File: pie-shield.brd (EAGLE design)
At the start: 25 x 25.2 mm, 20 parts, among them IC4 NRF24L01SMD, Q2 3.2X2.5CRYSTAL

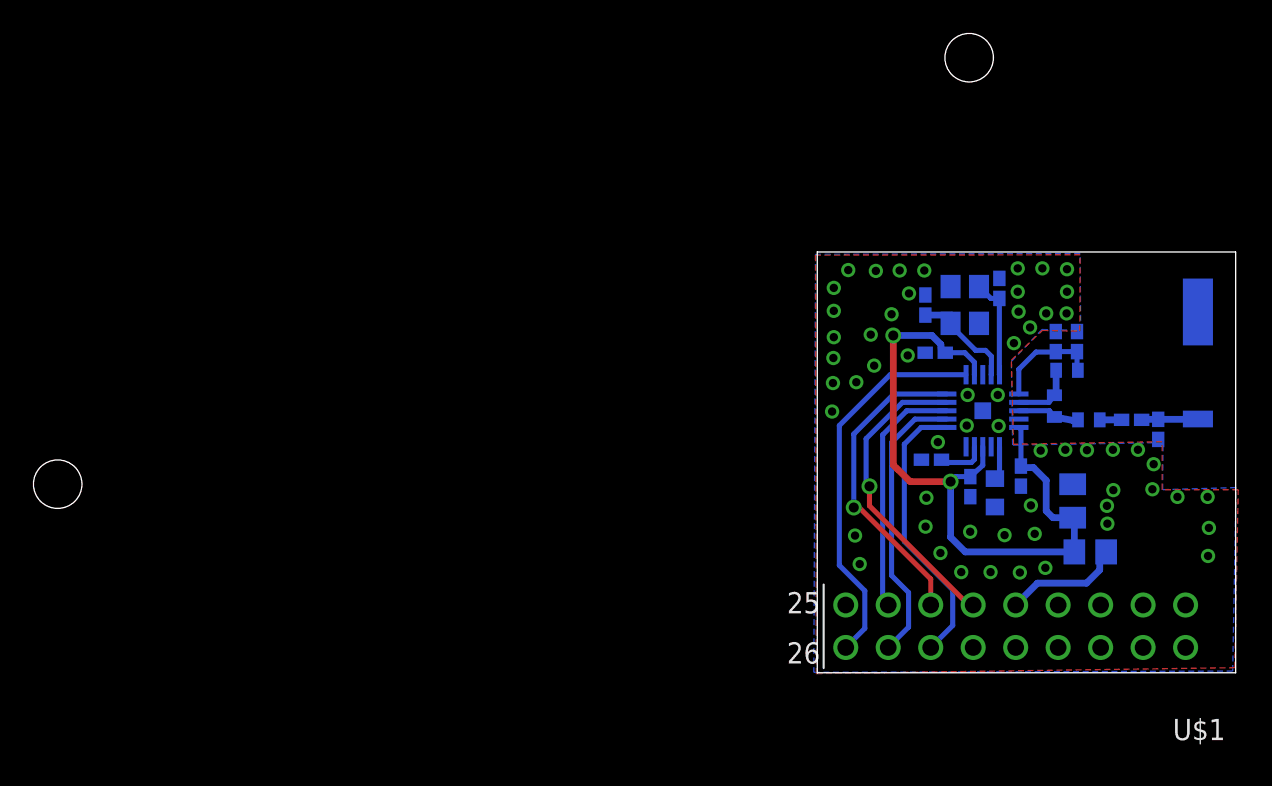
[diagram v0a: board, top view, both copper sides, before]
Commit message: fixed drill holes - removed
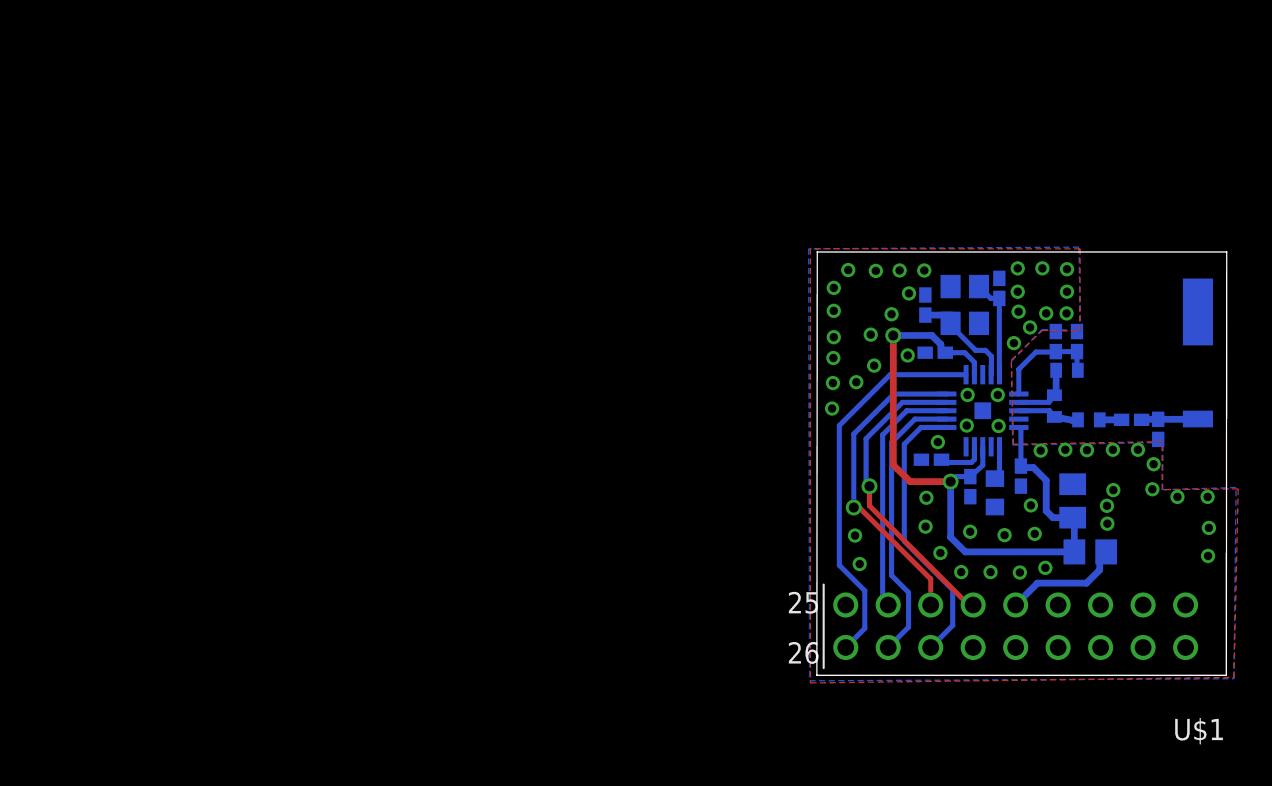
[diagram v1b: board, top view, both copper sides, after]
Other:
- board size 25 x 25.2 mm -> 24.5 x 25.3 mm
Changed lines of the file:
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@@
 <board>
 <plain>
-<wire x1="35.3314" y1="1.7526" x2="10.3152" y2="1.7526" width="0" layer="20"/>
-<wire x1="10.3152" y1="1.7526" x2="10.3152" y2="26.913" width="0" layer="20"/>
-<wire x1="10.3152" y1="26.913" x2="35.3314" y2="26.913" width="0" layer="20"/>
-<wire x1="35.3314" y1="26.913" x2="35.3314" y2="1.7526" width="0" layer="20"/>
+<wire x1="34.7726" y1="1.6002" x2="10.2898" y2="1.6002" width="0" layer="20"/>
+<wire x1="10.2898" y1="1.6002" x2="10.3152" y2="26.913" width="0" layer="20"/>
+<wire x1="10.3152" y1="26.913" x2="34.798" y2="26.913" width="0" layer="20"/>
+<wire x1="34.798" y1="26.913" x2="34.7726" y2="1.6002" width="0" layer="20"/>
 </plain>
 <attributes>
@@
 <vertex x="23.749" y="22.2758"/>
 <vertex x="26.0604" y="22.225"/>
-<vertex x="26.035" y="26.8224"/>
-<vertex x="10.2108" y="26.7716"/>
-<vertex x="10.1092" y="1.778"/>
-<vertex x="35.1536" y="1.8542"/>
+<vertex x="25.9588" y="27.2034"/>
+<vertex x="9.8044" y="27.1018"/>
+<vertex x="9.8552" y="1.27"/>
+<vertex x="35.2298" y="1.397"/>
 </polygon>
 <polygon width="0.3048" layer="1" thermals="no">
-<vertex x="10.2616" y="1.7018"/>
-<vertex x="35.2806" y="2.0574"/>
-<vertex x="35.4838" y="12.7"/>
+<vertex x="9.906" y="1.143"/>
+<vertex x="35.2298" y="1.4732"/>
+<vertex x="35.4838" y="12.7508"/>
 <vertex x="30.9372" y="12.7"/>
 <vertex x="30.9372" y="15.5702"/>
@@
 <vertex x="23.7744" y="22.225"/>
 <vertex x="26.0096" y="22.1742"/>
-<vertex x="26.035" y="26.7462"/>
-<vertex x="10.2108" y="26.7208"/>
+<vertex x="26.035" y="27.1018"/>
+<vertex x="9.906" y="27.1018"/>
 </polygon>
 <via x="22.352" y="23.3426" extent="1-16" drill="0.5" shape="octagon"/>
 <via x="23.7744" y="25.9334" extent="1-16" drill="0.5" shape="octagon"/>
 <via x="24.003" y="23.241" extent="1-16" drill="0.5" shape="octagon"/>
-<via x="11.2014" y="17.3736" extent="1-16" drill="0.5" shape="octagon"/>
+<via x="11.2014" y="17.5514" extent="1-16" drill="0.5" shape="octagon"/>
 <via x="12.573" y="9.9568" extent="1-16" drill="0.5" shape="octagon"/>
 <via x="33.655" y="12.2682" extent="1-16" drill="0.5" shape="octagon"/>
